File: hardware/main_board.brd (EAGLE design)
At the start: 109.9 x 68.6 mm, 112 parts, among them IC1 IC_USBLC6-2, IC2 LM1117IMPX-3.3, IC3 PIC32MX795F512, IC4 ENC28J60, IC5 LM1117MPX-2.5, U1 USD-SOCKETUSD, U2 VS1003, X2 CRYSTALS-NOGND-CFPX-217, X3 KUSBVX, Y1 CRYSTAL-GROUNDEDSMD-5X3.2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

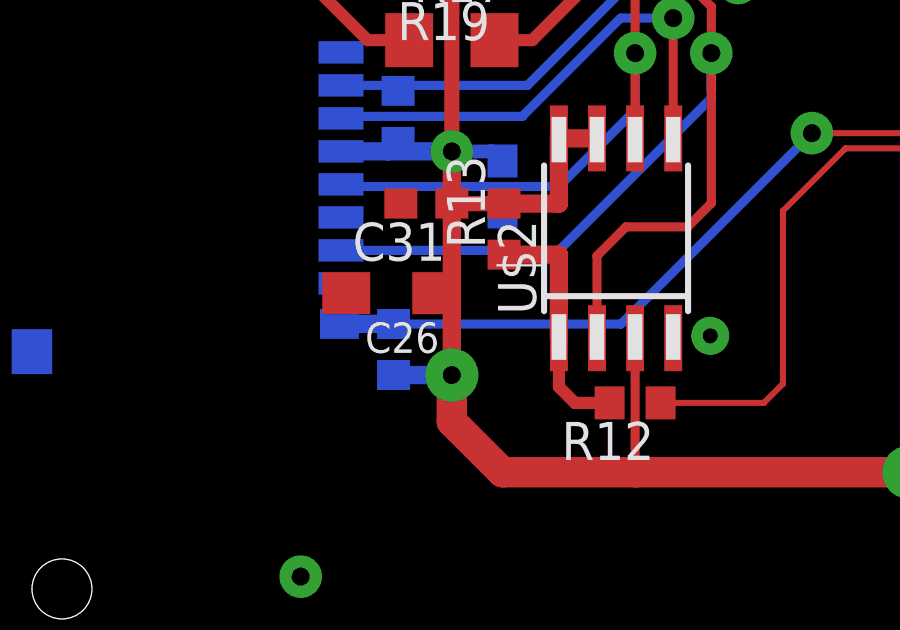
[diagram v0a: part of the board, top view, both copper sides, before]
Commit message: MISO pull-up added
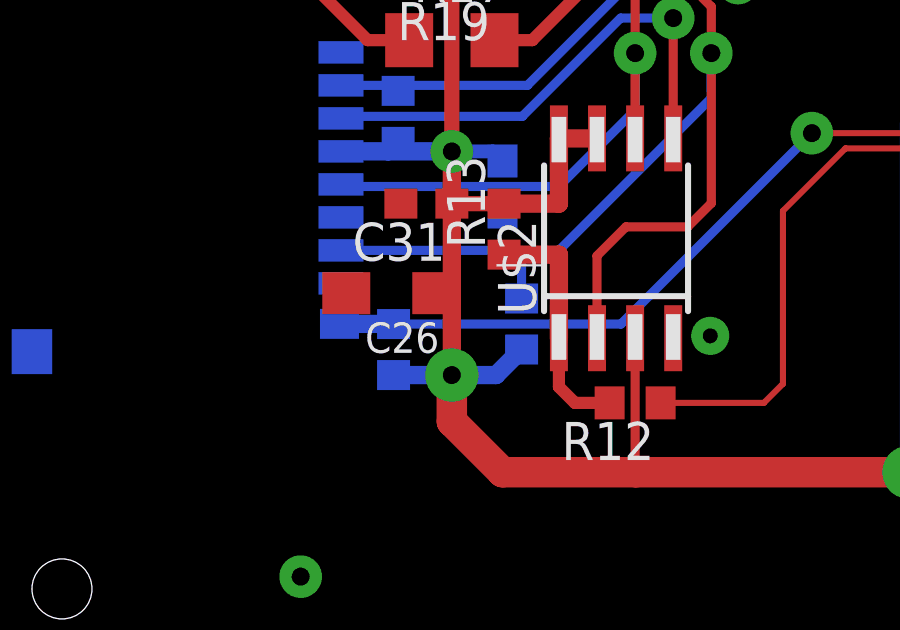
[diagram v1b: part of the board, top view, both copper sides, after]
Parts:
- added R14: (no value), rcl:R0603
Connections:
- net 3V: now also R14.2
- net MISO: now also R14.1
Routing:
- net 3V: track 443.9 -> 446.6 mm
- net MISO: track 60.8 -> 62.4 mm
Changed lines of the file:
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@@
 <attribute name="OC_FARNELL" value="unknown" x="80.899" y="10.795" size="1.778" layer="28" rot="MR180" display="off"/>
 </element>
+<element name="R14" library="rcl" package="R0603" value="" x="20.32" y="13.8294" rot="MR270"/>
 </elements>
 <signals>
@@
 <wire x1="63.754" y1="62.826" x2="63.754" y2="59.344" width="0.8128" layer="16"/>
 <wire x1="63.754" y1="59.344" x2="56.6928" y2="52.2828" width="0.8128" layer="16"/>
+<contactref element="R14" pad="2"/>
+<wire x1="17.995" y1="12.1294" x2="19.47" y2="12.1294" width="0.6096" layer="16"/>
+<wire x1="19.47" y1="12.1294" x2="20.32" y2="12.9794" width="0.6096" layer="16"/>
 <wire x1="17.741" y1="14.859" x2="17.4766" y2="14.859" width="0" layer="19" extent="1-1"/>
 </signal>
@@
 <wire x1="26.6446" y1="22.86" x2="26.6446" y2="17.8562" width="0.3048" layer="1"/>
 <wire x1="26.6446" y1="17.8562" x2="25.8572" y2="17.0688" width="0.3048" layer="1"/>
-<wire x1="14.3" y1="16.285" x2="21.5682" y2="16.285" width="0.3048" layer="16"/>
+<wire x1="14.3" y1="16.285" x2="20.32" y2="16.285" width="0.3048" layer="16"/>
+<wire x1="20.32" y1="16.285" x2="21.5682" y2="16.285" width="0.3048" layer="16"/>
 <wire x1="26.6446" y1="21.59" x2="26.6446" y2="22.86" width="0.3048" layer="16"/>
 <wire x1="21.5682" y1="16.285" x2="26.6446" y2="21.3614" width="0.3048" layer="16"/>
@@
 <wire x1="34.8996" y1="30.2514" x2="34.8996" y2="30.9626" width="0.2032" layer="1"/>
 <wire x1="34.584640625" y1="31.277559375" x2="34.8996" y2="30.9626" width="0.2032" layer="1"/>
+<contactref element="R14" pad="1"/>
+<wire x1="20.32" y1="14.6794" x2="20.32" y2="16.285" width="0.3048" layer="16"/>
 </signal>
 <signal name="MOSI">
